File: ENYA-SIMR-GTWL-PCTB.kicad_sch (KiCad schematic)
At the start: 15 parts, among them J1 PICO_BLADE_1x5_MALE_RA_SMD, J2 PICO_BLADE_1x5_MALE_RA_SMD, SW1 SKSTAJE010, SW2 SKSTAJE010, SW3 SKSTAJE010, SW4 SKSTAJE010, SW5 SKSTAJE010, SW6 SKSTAJE010

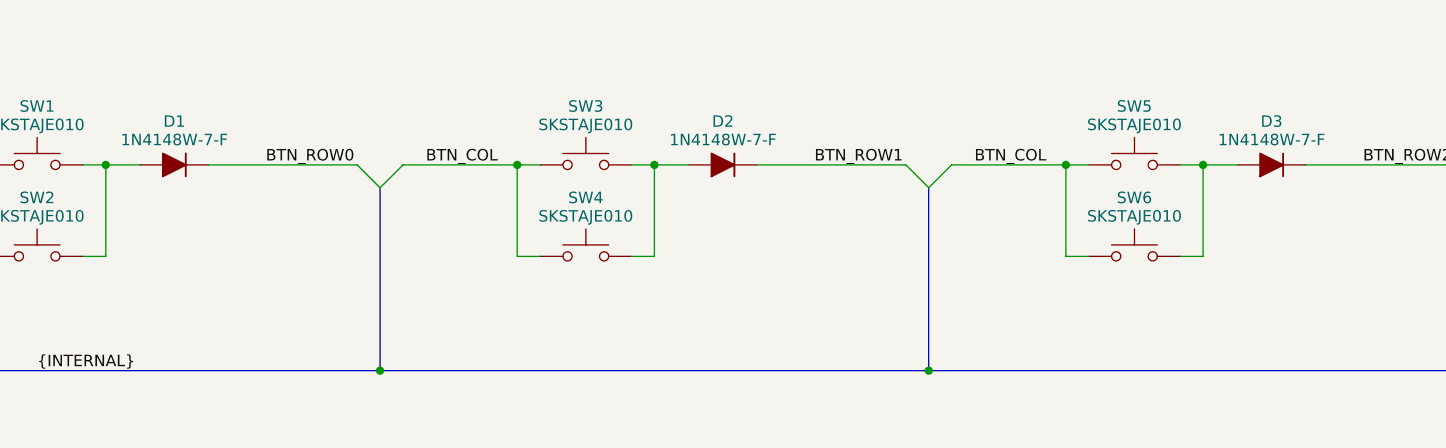
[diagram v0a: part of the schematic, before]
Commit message: correction button matrix diode polarity
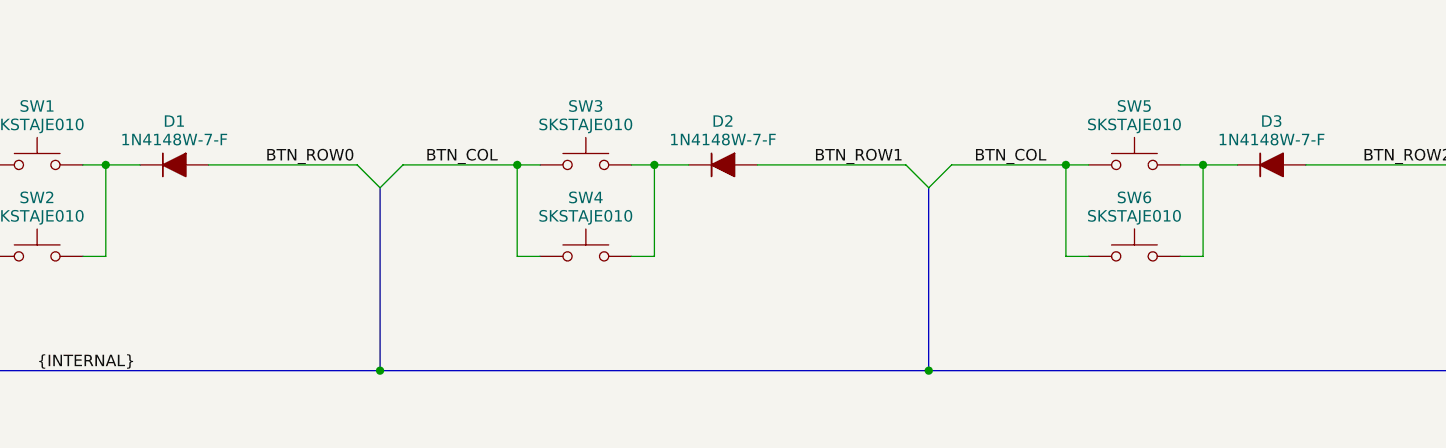
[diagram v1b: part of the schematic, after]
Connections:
- net BTN_ROW0: now also D1.2 (A); no longer D1.1 (K)
- net BTN_ROW1: now also D2.2 (A); no longer D2.1 (K)
- net BTN_ROW2: now also D3.2 (A); no longer D3.1 (K)
- net at SW1.2, SW2.2: now also D1.1 (K); no longer D1.2 (A)
- net at SW3.2, SW4.2: now also D2.1 (K); no longer D2.2 (A)
- net at SW5.2, SW6.2: now also D3.1 (K); no longer D3.2 (A)
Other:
- moved on the sheet: D1, D2, D3
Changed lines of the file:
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@@
     )
   )
-  (symbol (lib_id "ENYA_Diode_Rectifier:1N4148W-7-F_SOD-123") (at 228.6 111.76 180) (unit 1)
+  (symbol (lib_id "ENYA_Diode_Rectifier:1N4148W-7-F_SOD-123") (at 228.6 111.76 0) (unit 1)
     (in_bom yes) (on_board yes) (dnp no) (fields_autoplaced)
     (property "Reference" "D2" (at 228.6 106.9354 0)
@@
       (effects (font (size 1.27 1.27)))
     )
-    (property "Footprint" "Diode_SMD:D_SOD-123" (at 228.6 107.315 0)
+    (property "Footprint" "Diode_SMD:D_SOD-123" (at 228.6 116.205 0)
       (effects (font (size 1.27 1.27)) hide)
     )
@@
     )
   )
-  (symbol (lib_id "ENYA_Diode_Rectifier:1N4148W-7-F_SOD-123") (at 167.64 111.76 180) (unit 1)
+  (symbol (lib_id "ENYA_Diode_Rectifier:1N4148W-7-F_SOD-123") (at 167.64 111.76 0) (unit 1)
     (in_bom yes) (on_board yes) (dnp no) (fields_autoplaced)
     (property "Reference" "D1" (at 167.64 106.9354 0)
@@
       (effects (font (size 1.27 1.27)))
     )
-    (property "Footprint" "Diode_SMD:D_SOD-123" (at 167.64 107.315 0)
+    (property "Footprint" "Diode_SMD:D_SOD-123" (at 167.64 116.205 0)
       (effects (font (size 1.27 1.27)) hide)
     )
@@
     )
   )
-  (symbol (lib_id "ENYA_Diode_Rectifier:1N4148W-7-F_SOD-123") (at 289.56 111.76 180) (unit 1)
+  (symbol (lib_id "ENYA_Diode_Rectifier:1N4148W-7-F_SOD-123") (at 289.56 111.76 0) (unit 1)
     (in_bom yes) (on_board yes) (dnp no) (fields_autoplaced)
     (property "Reference" "D3" (at 289.56 106.9354 0)
@@
       (effects (font (size 1.27 1.27)))
     )
-    (property "Footprint" "Diode_SMD:D_SOD-123" (at 289.56 107.315 0)
-      (effects (font (size 1.27 1.27)) hide)
-    )
+    (property "Footprint" "Diode_SMD:D_SOD-123" (at 289.56 116.205 0)
+      (effects (font (size 1.27 1.27)) hide)
+    )

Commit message: WIP
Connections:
- net BTN_COL: now also J1.5 (Pin_5), J2.5 (Pin_5); no longer J1.1 (Pin_1), J2.1 (Pin_1)
- net BTN_ROW0: now also J1.4 (Pin_4), J2.4 (Pin_4); no longer J1.2 (Pin_2), J2.2 (Pin_2)
- net BTN_ROW2: now also J1.2 (Pin_2), J2.2 (Pin_2); no longer J1.4 (Pin_4), J2.4 (Pin_4)
- net GND: now also J1.1 (Pin_1), J2.1 (Pin_1); no longer J1.5 (Pin_5), J2.5 (Pin_5)
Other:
- moved on the sheet: J1, J2
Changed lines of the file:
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@@
     )
   )
-  (symbol (lib_id "ENYA_Connector_PicoBlade:PICO_BLADE_1x5_MALE_RA_SMD") (at 81.28 106.68 0) (mirror y) (unit 1)
-    (in_bom yes) (on_board yes) (dnp no) (fields_autoplaced)
-    (property "Reference" "J1" (at 81.28 96.75 0)
+  (symbol (lib_id "ENYA_Connector_PicoBlade:PICO_BLADE_1x5_MALE_RA_SMD") (at 81.28 106.68 180) (unit 1)
+    (in_bom yes) (on_board yes) (dnp no)
+    (property "Reference" "J1" (at 81.28 116.61 0)
       (effects (font (size 1.27 1.27)))
     )
-    (property "Value" "PICO_BLADE_1x5_MALE_RA_SMD" (at 81.28 114.3 0)
+    (property "Value" "PICO_BLADE_1x5_MALE_RA_SMD" (at 81.28 99.06 0)
       (effects (font (size 1.27 1.27)) hide)
     )
@@
       (effects (font (size 1.27 1.27)) hide)
     )
-    (property "Manufacturer Part Number" "532610571" (at 81.28 98.798 0)
+    (property "Manufacturer Part Number" "532610571" (at 81.28 114.562 0)
       (effects (font (size 1.27 1.27)))
     )
@@
     )
   )
-  (symbol (lib_id "ENYA_Connector_PicoBlade:PICO_BLADE_1x5_MALE_RA_SMD") (at 81.28 124.46 0) (mirror y) (unit 1)
-    (in_bom yes) (on_board yes) (dnp no) (fields_autoplaced)
-    (property "Reference" "J2" (at 81.28 114.53 0)
+  (symbol (lib_id "ENYA_Connector_PicoBlade:PICO_BLADE_1x5_MALE_RA_SMD") (at 81.28 124.46 180) (unit 1)
+    (in_bom yes) (on_board yes) (dnp no)
+    (property "Reference" "J2" (at 81.28 134.39 0)
       (effects (font (size 1.27 1.27)))
     )
-    (property "Value" "PICO_BLADE_1x5_MALE_RA_SMD" (at 81.28 132.08 0)
+    (property "Value" "PICO_BLADE_1x5_MALE_RA_SMD" (at 81.28 116.84 0)
       (effects (font (size 1.27 1.27)) hide)
     )
@@
       (effects (font (size 1.27 1.27)) hide)
     )
-    (property "Manufacturer Part Number" "532610571" (at 81.28 116.578 0)
+    (property "Manufacturer Part Number" "532610571" (at 81.28 132.342 0)
       (effects (font (size 1.27 1.27)))
     )
